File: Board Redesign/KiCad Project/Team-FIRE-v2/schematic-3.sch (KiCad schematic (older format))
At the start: 27 parts, among them IC1 MCP1826T-3302E_DC, IC2 BTS500601TEAAUMA2, J10 PCB.MMCX.F.ST.SMT.JACK.HT, J6 Conn_01x03, J7 Conn_01x03, J8 Conn_01x02, J9 U.FL-R-SMT_10_, U8 TPS82140

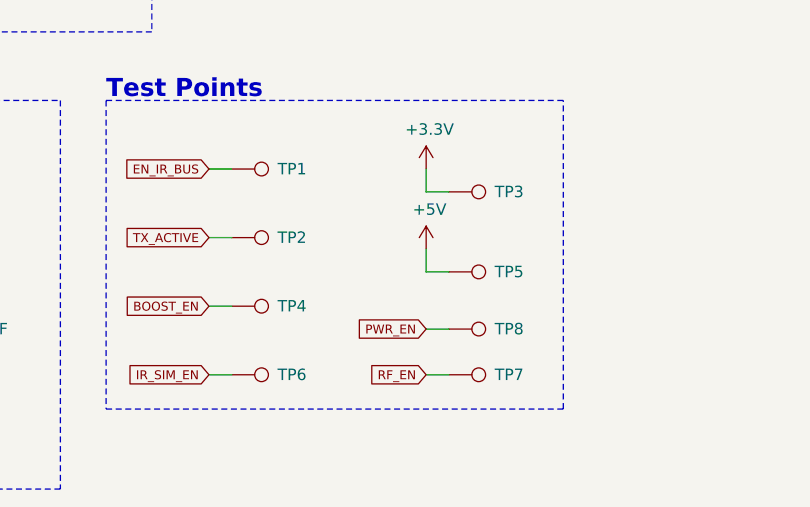
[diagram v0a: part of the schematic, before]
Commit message: Finished PCB
- Added various 3D models for a complete 3D visualization of the PCB
- Generated a finalized netlist
- Fixed misnamed net from IR_SIM_RST to IR_SIM_RESET
- Finished all component placement for the PCB; the only work remaining are the mounting holes, and the grounding vias for the IRIDIUM
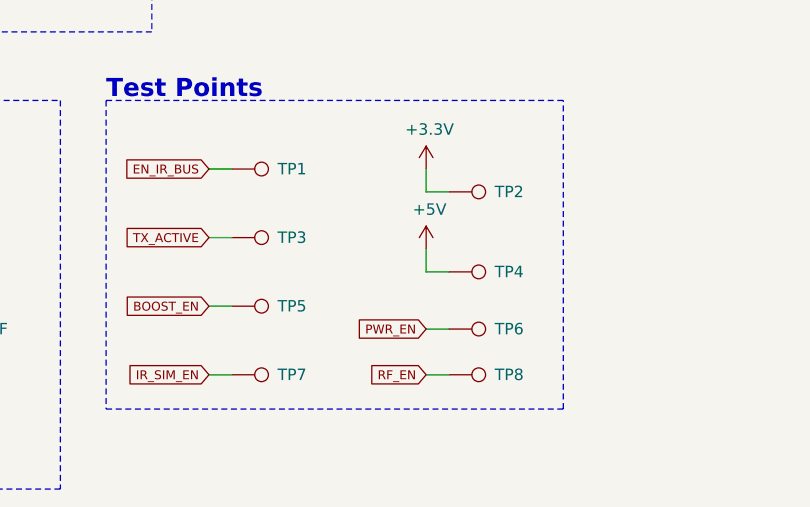
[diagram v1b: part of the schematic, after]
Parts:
- IC2: Manufacturer (none) -> Infineon; Manufacturer_Name Infineon -> (none); Mouser Part Number 726-BTS500601TEAAUMA -> (none); Mouser Price/Stock https://www.mouser.com/Search/Refine.aspx?Keyword=726-BTS50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 -> (none); Supplier (none) -> Mouser; Supplier PN (none) -> 726-BTS500601TEAAUMA
- TP1, TP2, TP3, TP4, TP5, TP6, TP7, TP8: footprint TestPoint:TestPoint_Pad_D1.5mm -> TestPoint:TestPoint_Pad_D1.0mm
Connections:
- net +3V3: now also TP2.1; no longer TP3.1
- net +5V: now also TP4.1; no longer TP5.1
- net BOOST_EN: now also TP5.1; no longer TP4.1
- net IR_SIM_EN: now also TP7.1; no longer TP6.1
- net PWR_EN: now also TP6.1; no longer TP8.1
- net RF_EN: now also TP8.1; no longer TP7.1
- net TX_ACTIVE: now also TP3.1; no longer TP2.1
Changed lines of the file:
@@
 F 4 "INFINEON - BTS500601TEAAUMA2 - Power Load Switch, AEC-Q100, High Side, 1 Output, 13.5 V, 60 A/0.0068 ohm out, TO-252-5" H 2950 1100 50  0001 L CNN "Description"
 F 5 "2.4" H 2950 1000 50  0001 L CNN "Height"
-F 6 "Infineon" H 2950 900 50  0001 L CNN "Manufacturer_Name"
+F 6 "Infineon" H 2950 900 50  0001 L CNN "Manufacturer"
 F 7 "BTS500601TEAAUMA2" H 2950 800 50  0001 L CNN "MPN"
-F 8 "726-BTS500601TEAAUMA" H 2950 700 50  0001 L CNN "Mouser Part Number"
-F 9 "https://www.mouser.com/Search/Refine.aspx?Keyword=726-BTS500601TEAAUMA" H 2950 600 50  0001 L CNN "Mouser Price/Stock"
+F 8 "726-BTS500601TEAAUMA" H 2950 700 50  0001 L CNN "Supplier PN"
+F 9 "Mouser" H 2950 600 50  0001 L CNN "Supplier"
 	1    2100 1200
 	1    0    0    -1
@@
 F 0 "TP1" V 4050 3100 50  0000 L CNN
 F 1 "TestPoint" V 4095 3088 50  0001 L CNN
-F 2 "TestPoint:TestPoint_Pad_D1.5mm" H 4250 2900 50  0001 C CNN
+F 2 "TestPoint:TestPoint_Pad_D1.0mm" H 4250 2900 50  0001 C CNN
 F 3 "~" H 4250 2900 50  0001 C CNN
 	1    4050 2900
@@
 Text GLabel 3950 2900 0    39   Input ~ 0
 EN_IR_BUS
-$Comp
-L Connector:TestPoint TP2
-U 1 1 5EAE78B2
-P 4050 3200
-F 0 "TP2" V 4050 3400 50  0000 L CNN
-F 1 "TestPoint" V 4095 3388 50  0001 L CNN
-F 2 "TestPoint:TestPoint_Pad_D1.5mm" H 4250 3200 50  0001 C CNN
-F 3 "~" H 4250 3200 50  0001 C CNN
-	1    4050 3200
-	0    1    1    0
-$EndComp
-$Comp
-L Connector:TestPoint TP4
-U 1 1 5EAE8FA8
-P 4050 3500
-F 0 "TP4" V 4050 3700 50  0000 L CNN
-F 1 "TestPoint" V 4095 3688 50  0001 L CNN
-F 2 "TestPoint:TestPoint_Pad_D1.5mm" H 4250 3500 50  0001 C CNN
-F 3 "~" H 4250 3500 50  0001 C CNN
-	1    4050 3500
-	0    1    1    0
-$EndComp
 Text GLabel 3950 3200 0    39   Input ~ 0
 TX_ACTIVE
 Text GLabel 3950 3500 0    39   Input ~ 0
 BOOST_EN
-$Comp
-L Connector:TestPoint TP3
-U 1 1 5EB00868
-P 5000 3000
-F 0 "TP3" V 5000 3200 50  0000 L CNN
-F 1 "TestPoint" V 5045 3188 50  0001 L CNN
-F 2 "TestPoint:TestPoint_Pad_D1.5mm" H 5200 3000 50  0001 C CNN
-F 3 "~" H 5200 3000 50  0001 C CNN
-	1    5000 3000
-	0    1    1    0
-$EndComp
-$Comp
-L Connector:TestPoint TP6
-U 1 1 5EB00870
-P 4050 3800
-F 0 "TP6" V 4050 4000 50  0000 L CNN
-F 1 "TestPoint" V 4095 3988 50  0001 L CNN
-F 2 "TestPoint:TestPoint_Pad_D1.5mm" H 4250 3800 50  0001 C CNN
-F 3 "~" H 4250 3800 50  0001 C CNN
-	1    4050 3800
-	0    1    1    0
-$EndComp
-$Comp
-L Connector:TestPoint TP7
-U 1 1 5EB00877
-P 5000 3800
-F 0 "TP7" V 5000 4000 50  0000 L CNN
-F 1 "TestPoint" V 5045 3988 50  0001 L CNN
-F 2 "TestPoint:TestPoint_Pad_D1.5mm" H 5200 3800 50  0001 C CNN
-F 3 "~" H 5200 3800 50  0001 C CNN
-	1    5000 3800
-	0    1    1    0
-$EndComp
 Text GLabel 4900 3800 0    39   Input ~ 0
 RF_EN
@@
 $EndComp
 $Comp
-L Connector:TestPoint TP5
-U 1 1 5EB07A7D
-P 5000 3350
-F 0 "TP5" V 5000 3550 50  0000 L CNN
-F 1 "TestPoint" V 5045 3538 50  0001 L CNN
-F 2 "TestPoint:TestPoint_Pad_D1.5mm" H 5200 3350 50  0001 C CNN
-F 3 "~" H 5200 3350 50  0001 C CNN
-	1    5000 3350
-	0    1    1    0
-$EndComp
-$Comp
 L power:+5V #PWR0176
 U 1 1 5EB0D55E
@@
 Text GLabel 3950 3800 0    39   Input ~ 0
 IR_SIM_EN
-$Comp
-L Connector:TestPoint TP8
-U 1 1 5EB13EEF
-P 5000 3600
-F 0 "TP8" V 5000 3800 50  0000 L CNN
-F 1 "TestPoint" V 5045 3788 50  0001 L CNN
-F 2 "TestPoint:TestPoint_Pad_D1.5mm" H 5200 3600 50  0001 C CNN
-F 3 "~" H 5200 3600 50  0001 C CNN
-	1    5000 3600
-	0    1    1    0
-$EndComp
 Text GLabel 4900 3600 0    39   Input ~ 0
 PWR_EN
@@
 Wire Wire Line
 	2250 3100 2550 3100
+$Comp
+L Connector:TestPoint TP3
+U 1 1 5ECCDBCF
+P 4050 3200
+F 0 "TP3" V 4050 3400 50  0000 L CNN
+F 1 "TestPoint" V 4095 3388 50  0001 L CNN
+F 2 "TestPoint:TestPoint_Pad_D1.0mm" H 4250 3200 50  0001 C CNN
+F 3 "~" H 4250 3200 50  0001 C CNN
+	1    4050 3200
+	0    1    1    0
+$EndComp
+$Comp
+L Connector:TestPoint TP5
+U 1 1 5ECCDECD
+P 4050 3500
+F 0 "TP5" V 4050 3700 50  0000 L CNN
+F 1 "TestPoint" V 4095 3688 50  0001 L CNN
+F 2 "TestPoint:TestPoint_Pad_D1.0mm" H 4250 3500 50  0001 C CNN
+F 3 "~" H 4250 3500 50  0001 C CNN
+	1    4050 3500
+	0    1    1    0
+$EndComp
+$Comp
+L Connector:TestPoint TP7
+U 1 1 5ECCE29C
+P 4050 3800
+F 0 "TP7" V 4050 4000 50  0000 L CNN
+F 1 "TestPoint" V 4095 3988 50  0001 L CNN
+F 2 "TestPoint:TestPoint_Pad_D1.0mm" H 4250 3800 50  0001 C CNN
+F 3 "~" H 4250 3800 50  0001 C CNN
+	1    4050 3800
+	0    1    1    0
+$EndComp
+$Comp
+L Connector:TestPoint TP2
+U 1 1 5ECCE502
+P 5000 3000
+F 0 "TP2" V 5000 3200 50  0000 L CNN
+F 1 "TestPoint" V 5045 3188 50  0001 L CNN
+F 2 "TestPoint:TestPoint_Pad_D1.0mm" H 5200 3000 50  0001 C CNN
+F 3 "~" H 5200 3000 50  0001 C CNN
+	1    5000 3000
+	0    1    1    0
+$EndComp
+$Comp
+L Connector:TestPoint TP4
+U 1 1 5ECCE885
+P 5000 3350
+F 0 "TP4" V 5000 3550 50  0000 L CNN
+F 1 "TestPoint" V 5045 3538 50  0001 L CNN
+F 2 "TestPoint:TestPoint_Pad_D1.0mm" H 5200 3350 50  0001 C CNN
+F 3 "~" H 5200 3350 50  0001 C CNN
+	1    5000 3350
+	0    1    1    0
+$EndComp
+$Comp
+L Connector:TestPoint TP6
+U 1 1 5ECCEAEB
+P 5000 3600
+F 0 "TP6" V 5000 3800 50  0000 L CNN
+F 1 "TestPoint" V 5045 3788 50  0001 L CNN
+F 2 "TestPoint:TestPoint_Pad_D1.0mm" H 5200 3600 50  0001 C CNN
+F 3 "~" H 5200 3600 50  0001 C CNN
+	1    5000 3600
+	0    1    1    0
+$EndComp
+$Comp
+L Connector:TestPoint TP8
+U 1 1 5ECCEDE9
+P 5000 3800
+F 0 "TP8" V 5000 4000 50  0000 L CNN
+F 1 "TestPoint" V 5045 3988 50  0001 L CNN
+F 2 "TestPoint:TestPoint_Pad_D1.0mm" H 5200 3800 50  0001 C CNN
+F 3 "~" H 5200 3800 50  0001 C CNN
+	1    5000 3800
+	0    1    1    0
+$EndComp
 $EndSCHEMATC
